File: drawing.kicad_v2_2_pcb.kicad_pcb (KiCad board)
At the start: 2 copper layers, 93 x 65 mm, 40 parts, among them IC1 DW01A-G, J1 Micro USB Chargeport, J2 Prog headers, J3 128x32 I2C OLED, J4 TP4056, J5 MK-12C02, J6 Conn_01x02, Q1 FS8205, U1 HT7333-SOT89, U2 ESP-12E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

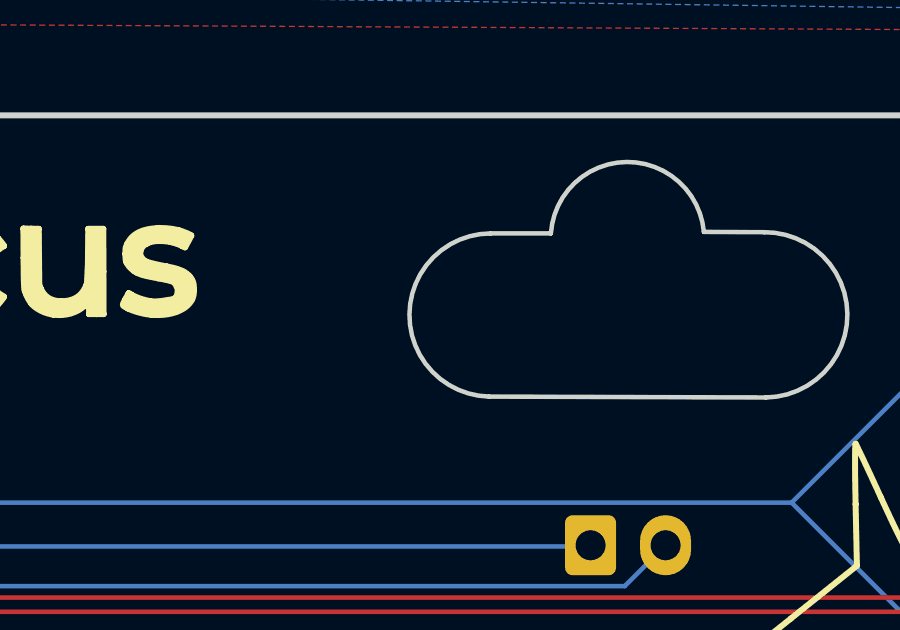
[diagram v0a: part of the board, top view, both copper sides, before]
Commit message: Fixed esp8266 programming circuit in v3.0
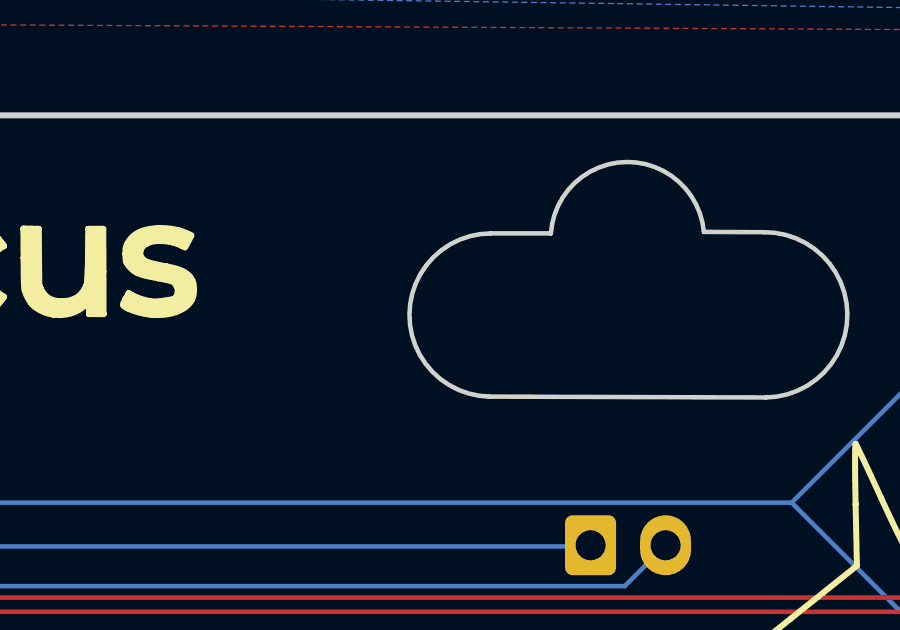
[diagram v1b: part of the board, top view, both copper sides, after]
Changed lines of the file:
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@@
   (gr_curve (pts (xy 106.009996 63.449159) (xy 106.009996 62.330545) (xy 107.347998 61.43) (xy 109.01 61.43)) (layer "Edge.Cuts") (width 0.2))
   (gr_line (start 147.916669 65.364807) (end 149.92662 65.364873) (layer "Edge.Cuts") (width 0.15))
-  (gr_arc (start 147.86662 70.804873) (mid 145.211616 68.060184) (end 147.916669 65.364807) (layer "Edge.Cuts") (width 0.15))
+  (gr_arc (start 147.86662 70.804873) (mid 145.211618 68.060184) (end 147.916669 65.364807) (layer "Edge.Cuts") (width 0.15))
   (gr_line (start 106.009996 124.410835) (end 106.009996 63.449159) (layer "Edge.Cuts") (width 0.2))
   (gr_line (start 157.09662 70.834873) (end 147.86662 70.804873) (layer "Edge.Cuts") (width 0.15))
